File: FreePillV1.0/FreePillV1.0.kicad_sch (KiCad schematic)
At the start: 2 parts

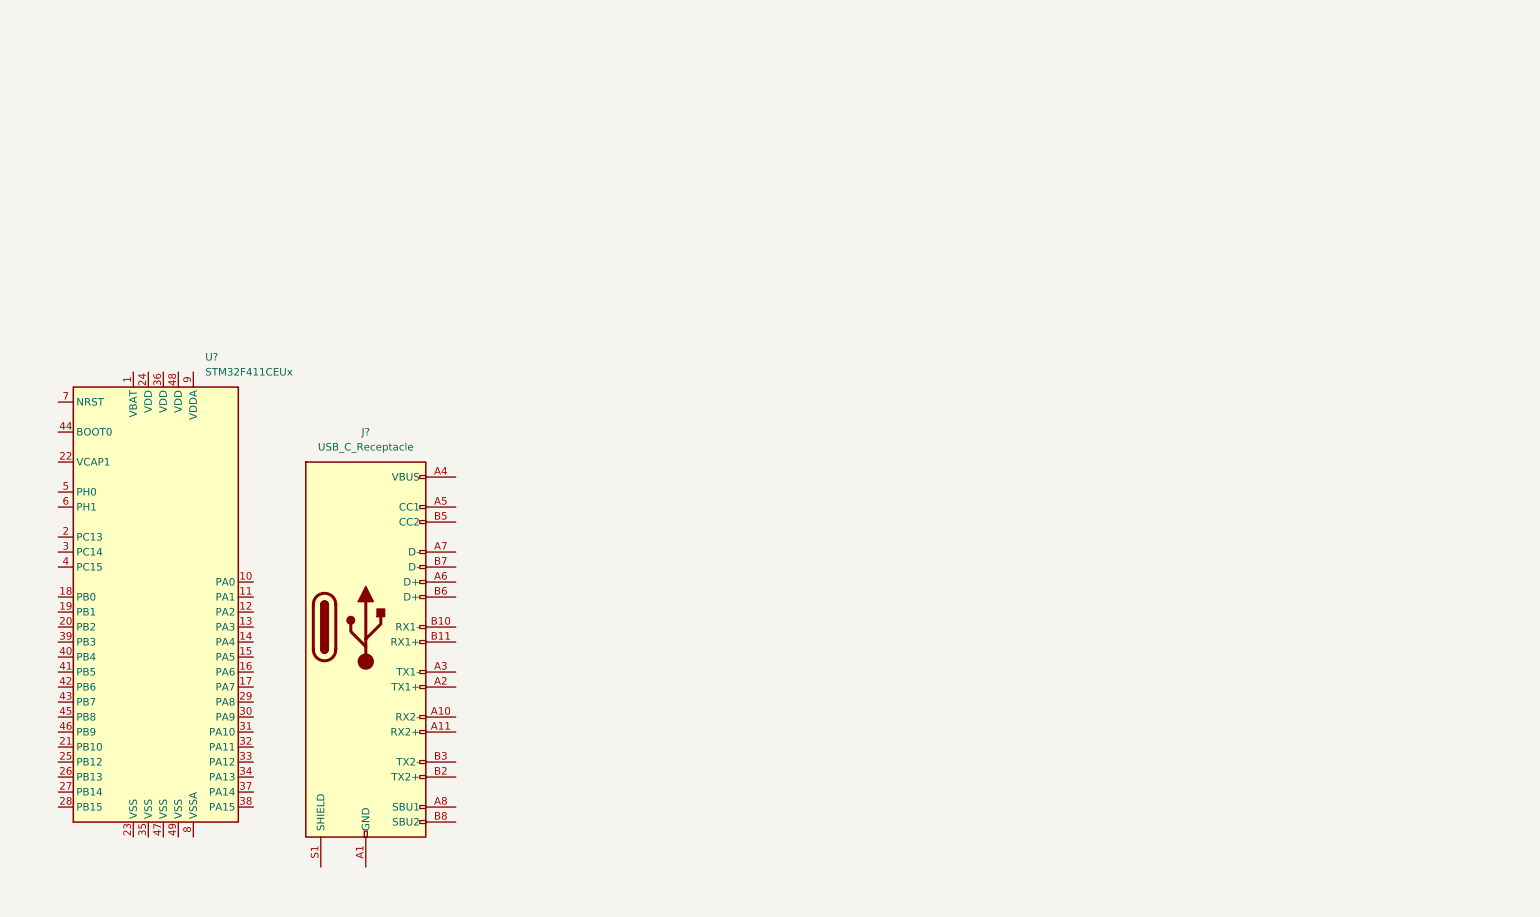
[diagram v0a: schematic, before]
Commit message: completed usb c 2.0 port wiring
(subject to change, posted for confirmation)
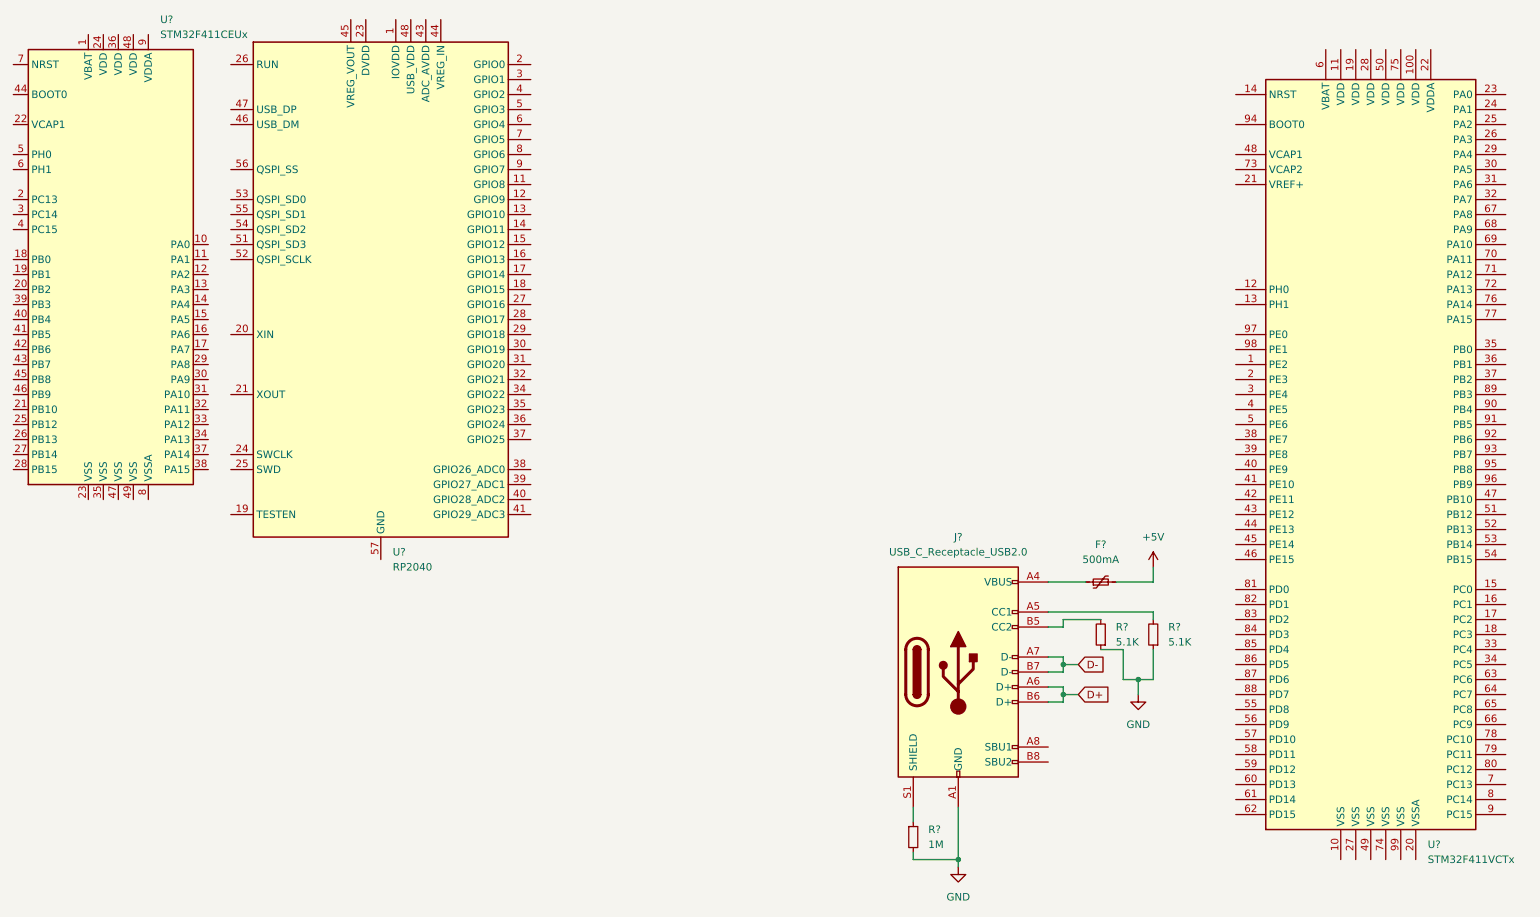
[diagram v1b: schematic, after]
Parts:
- removed J?: USB_C_Receptacle, symbol Connector:USB_C_Receptacle
- added F?: 500mA, symbol Device:Polyfuse_Small
- added J?: USB_C_Receptacle_USB2.0, symbol Connector:USB_C_Receptacle_USB2.0
- added R? (x2): 5.1K, symbol Device:R_Small
- added R?: 1M, symbol Device:R_Small
- added U?: RP2040, Package_DFN_QFN:QFN-56-1EP_7x7mm_P0.4mm_EP3.2x3.2mm, symbol MCU_RaspberryPi:RP2040
- added U?: STM32F411VCTx, Package_QFP:LQFP-100_14x14mm_P0.5mm, symbol MCU_ST_STM32F4:STM32F411VCTx
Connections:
- new net: J?.B5 (CC2), R?.2
- new net: F?.1, J?.A4 (VBUS), J?.A9 (VBUS), J?.B4 (VBUS), J?.B9 (VBUS)
- new net: U?.1 (IOVDD), U?.10 (IOVDD), U?.22 (IOVDD), U?.33 (IOVDD), U?.42 (IOVDD), U?.49 (IOVDD)
- new net: U?.23 (DVDD), U?.50 (DVDD)
- new net: J?.A5 (CC1), R?.2
- new net: J?.S1 (SHIELD), R?.1
- new net +5V: F?.2
- new net D+: J?.A6 (D+), J?.B6 (D+)
- new net D-: J?.A7 (D-), J?.B7 (D-)
- new net GND: J?.A1 (GND), J?.A12 (GND), J?.B1 (GND), J?.B12 (GND), R?.1, R?.1, R?.2
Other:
- moved on the sheet: U?

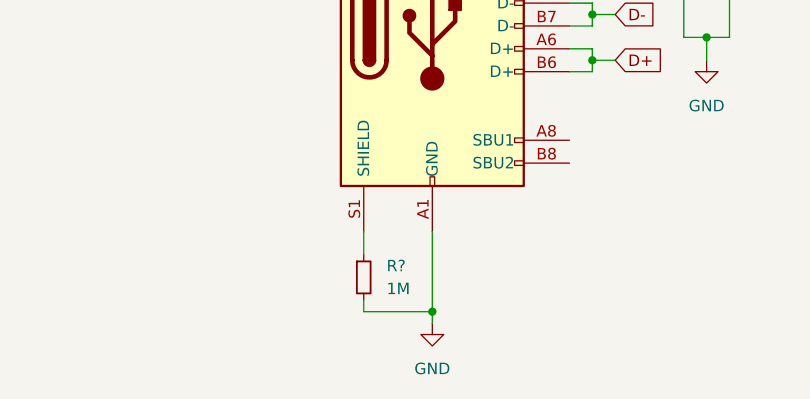
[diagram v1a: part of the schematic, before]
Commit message: removed 1M shield resistor
don't trust everything you see online kids
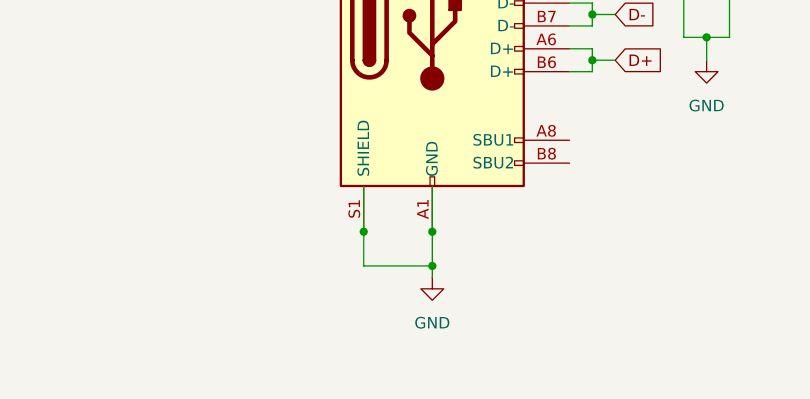
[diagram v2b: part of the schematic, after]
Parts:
- removed R?: 1M, symbol Device:R_Small
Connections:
- net GND: now also J?.S1 (SHIELD)
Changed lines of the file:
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@@
 (kicad_sch (version 20211123) (generator eeschema)
   (paper "A4")
-  (junction (at 177.8 157.48) (diameter 0) (color 0 0 0 0)
+  (junction (at 177.8 152.4) (diameter 0) (color 0 0 0 0)
   )
   (junction (at 195.58 124.46) (diameter 0) (color 0 0 0 0)
@@
   (junction (at 208.28 127) (diameter 0) (color 0 0 0 0)
   )
+  (junction (at 177.8 148.59) (diameter 0) (color 0 0 0 0)
+  )
   (junction (at 195.58 129.54) (diameter 0) (color 0 0 0 0)
   )
+  (junction (at 170.18 148.59) (diameter 0) (color 0 0 0 0)
+  )
   (wire (pts (xy 208.28 127) (xy 208.28 129.54))
     (stroke (width 0) (type default) (color 0 0 0 0))
   )
-  (wire (pts (xy 170.18 148.59) (xy 170.18 151.13))
-    (stroke (width 0) (type default) (color 0 0 0 0))
-  )
   (wire (pts (xy 195.58 123.19) (xy 193.04 123.19))
     (stroke (width 0) (type default) (color 0 0 0 0))
@@
     (stroke (width 0) (type default) (color 0 0 0 0))
   )
-  (wire (pts (xy 177.8 148.59) (xy 177.8 157.48))
+  (wire (pts (xy 177.8 143.51) (xy 177.8 148.59))
     (stroke (width 0) (type default) (color 0 0 0 0))
   )
@@
     (stroke (width 0) (type default) (color 0 0 0 0))
   )
+  (wire (pts (xy 170.18 148.59) (xy 170.18 152.4))
+    (stroke (width 0) (type default) (color 0 0 0 0))
+  )
   (wire (pts (xy 201.93 121.92) (xy 205.74 121.92))
     (stroke (width 0) (type default) (color 0 0 0 0))
   )
-  (wire (pts (xy 170.18 156.21) (xy 170.18 157.48))
+  (wire (pts (xy 170.18 143.51) (xy 170.18 148.59))
     (stroke (width 0) (type default) (color 0 0 0 0))
   )
@@
     (stroke (width 0) (type default) (color 0 0 0 0))
   )
-  (wire (pts (xy 177.8 157.48) (xy 177.8 158.75))
+  (wire (pts (xy 177.8 152.4) (xy 177.8 153.67))
+    (stroke (width 0) (type default) (color 0 0 0 0))
+  )
+  (wire (pts (xy 177.8 148.59) (xy 177.8 152.4))
     (stroke (width 0) (type default) (color 0 0 0 0))
   )
@@
     (stroke (width 0) (type default) (color 0 0 0 0))
   )
-  (wire (pts (xy 170.18 157.48) (xy 177.8 157.48))
+  (wire (pts (xy 170.18 152.4) (xy 177.8 152.4))
     (stroke (width 0) (type default) (color 0 0 0 0))
   )
@@
     (pin "1")
   )
-  (symbol (lib_id "power:GND") (at 177.8 158.75 0) (unit 1)
-    (in_bom yes) (on_board yes) (fields_autoplaced)
-    (property "Reference" "#PWR?" (id 0) (at 177.8 165.1 0)
-      (effects (font (size 1.27 1.27)) hide)
-    )
-    (property "Value" "GND" (id 1) (at 177.8 163.83 0))
-    (property "Footprint" "" (id 2) (at 177.8 158.75 0)
-      (effects (font (size 1.27 1.27)) hide)
-    )
-    (property "Datasheet" "" (id 3) (at 177.8 158.75 0)
+  (symbol (lib_id "power:GND") (at 177.8 153.67 0) (unit 1)
+    (in_bom yes) (on_board yes) (fields_autoplaced)
+    (property "Reference" "#PWR?" (id 0) (at 177.8 160.02 0)
+      (effects (font (size 1.27 1.27)) hide)
+    )
+    (property "Value" "GND" (id 1) (at 177.8 158.75 0))
+    (property "Footprint" "" (id 2) (at 177.8 153.67 0)
+      (effects (font (size 1.27 1.27)) hide)
+    )
+    (property "Datasheet" "" (id 3) (at 177.8 153.67 0)
       (effects (font (size 1.27 1.27)) hide)
     )
@@
     (pin "99")
   )
-  (symbol (lib_id "Device:R_Small") (at 170.18 153.67 0) (unit 1)
-    (in_bom yes) (on_board yes) (fields_autoplaced)
-    (property "Reference" "R?" (id 0) (at 172.72 152.3999 0)
-      (effects (font (size 1.27 1.27)) (justify left))
-    )
-    (property "Value" "1M" (id 1) (at 172.72 154.9399 0)
-      (effects (font (size 1.27 1.27)) (justify left))
-    )
-    (property "Footprint" "" (id 2) (at 170.18 153.67 0)
-      (effects (font (size 1.27 1.27)) hide)
-    )
-    (property "Datasheet" "~" (id 3) (at 170.18 153.67 0)
-      (effects (font (size 1.27 1.27)) hide)
-    )
-    (pin "1")
-    (pin "2")
-  )
   (sheet_instances
     (path "/" (page "1"))
@@
       (reference "R?") (unit 1) (value "5.1K") (footprint "")
     )
-    (path "/fca5f28d-5e14-4c82-b2e8-cb07499c2a9b"
-      (reference "R?") (unit 1) (value "1M") (footprint "")
-    )
     (path "/7b7b3cdf-fea5-4e38-9058-2ce5dabb2257"
